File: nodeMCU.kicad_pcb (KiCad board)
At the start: 2 copper layers, 27 x 50 mm, 40 parts, among them J1 USB_B_Micro, J2 Conn_01x15, J3 Conn_01x15, Q1 S8050, Q2 S8050, U1 AP1117-33, U2 CP2102N-A01-GQFN28, U3 ESP-12E

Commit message: PCB Terminado
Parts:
- moved H3 39.7 mm to (158.0, 65.8)
- moved H4 39.7 mm to (134.6, 65.7)
- moved C3 39.5 mm to (141.6, 94.2)
- moved C4 39.5 mm to (143.8, 102.5)
- moved C6 39.5 mm to (141.6, 90.3)
- moved C8 39.5 mm to (136.6, 68.7)
- moved D1 39.5 mm to (138.7, 102.7)
- moved R12 39.5 mm to (155.2, 90.0)
- moved R13 39.5 mm to (136.6, 72.2)
- moved R14 39.5 mm to (136.6, 74.2)
- moved R3 39.5 mm to (149.8, 97.3)
- moved R4 39.5 mm to (144.3, 97.3)
- moved R6 39.5 mm to (140.7, 97.3)
- moved R7 39.5 mm to (153.5, 97.3)
- moved REF** 39.5 mm to (146.2, 73.3)
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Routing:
- net GND: vias 106 -> 107
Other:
- board text added: "Esta placa fue desarrollada en el marco de la materia "Diseño de circuitos impresos" pertenceciente a la Carrera de Especializacion en Sistemas Embebidos de la UBA. Para este proyecto se tomo como premisa usar los mismo tamaños que su original. Es por esto que algunos de los componentes poseen encapsulados de tamaño reducido. Grillas: 1mm, 0.5mm, 0.10mm Vias: 0.30/0.15mm, 0.5/0.3mm Margen: 0.2mm 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"

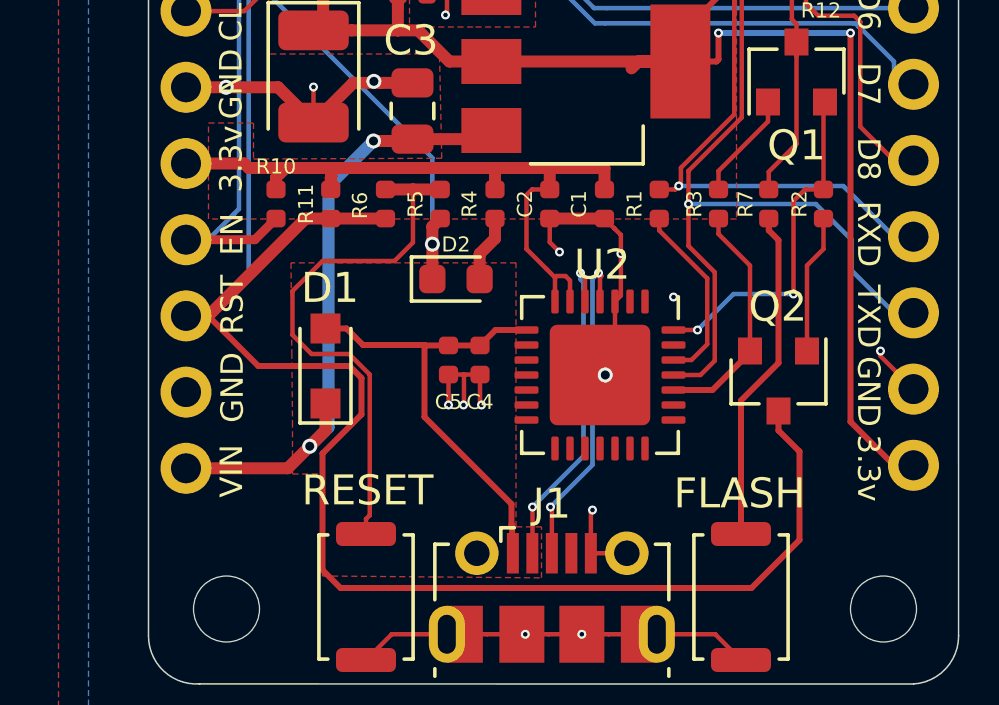
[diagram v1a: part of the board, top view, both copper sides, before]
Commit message: Agrego fiducial
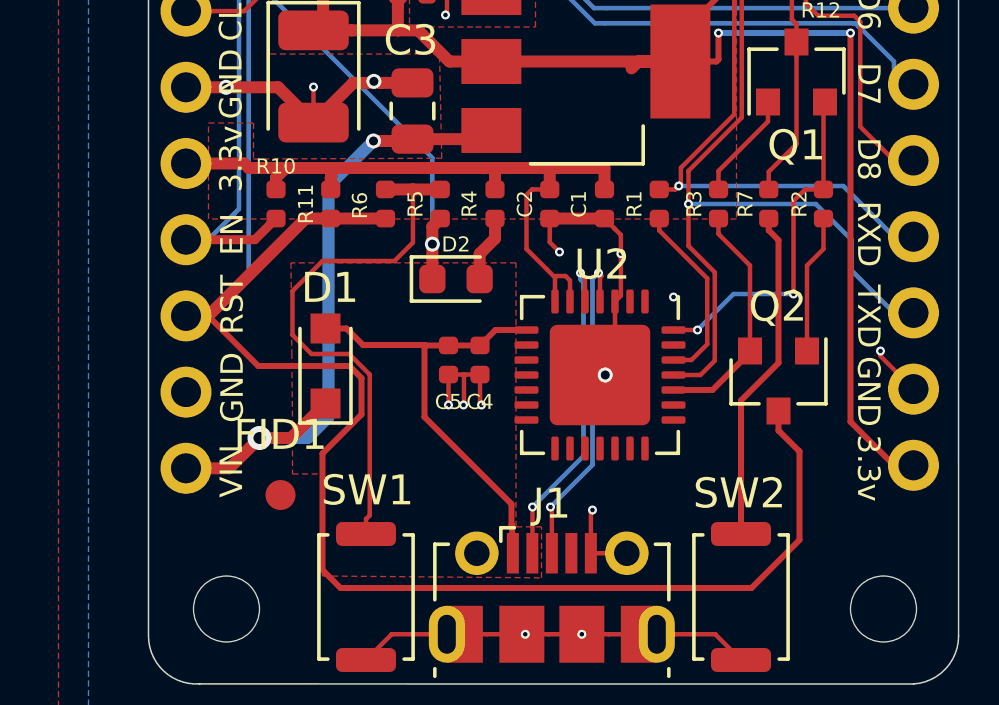
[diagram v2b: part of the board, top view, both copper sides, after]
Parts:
- added FID1: Fiducial, Fiducial:Fiducial_1mm_Mask2mm, F.Cu at (137.2, 107.0)
- renumbered RESET to SW1, FLASH to SW2
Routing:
- net +5V: track 20.5 -> 22.0 mm

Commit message: Terminado el PCB
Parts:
- moved R9 0.16 mm to (156.0, 82.2)
- moved R2 0.13 mm to (155.4, 97.4)
- moved R8 0.07 mm to (156.0, 80.0)
- moved R10 0.05 mm to (137.0, 97.3)

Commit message: Agrego comentarios del Docente
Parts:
- moved H2 7.91 mm to (127.5, 110.5)
- moved H4 7.63 mm to (127.0, 65.0)
- moved J2 7.07 mm to (127.0, 69.5)
- moved C1 7.07 mm to (141.0, 96.3)
- moved C2 7.07 mm to (139.2, 96.3)
- moved C3 7.07 mm to (134.6, 93.2)
- moved C4 7.07 mm to (136.8, 101.5)
- moved C5 7.07 mm to (135.8, 101.5)
- moved C6 7.07 mm to (134.6, 89.3)
- moved C7 7.07 mm to (131.3, 92.0)
- moved C8 7.07 mm to (129.6, 67.7)
- moved D1 7.07 mm to (131.7, 101.7)
- moved D2 7.07 mm to (136.1, 98.8)
- moved FID1 7.07 mm to (130.2, 106.0)
- moved J3 7.07 mm to (151.3, 69.5)
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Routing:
- net /nRST: track 77.2 -> 79.1 mm
- net /GPIO_2: track 4.42 -> 3.12 mm
- net Net-(J1-Pad2): track 11.1 -> 12.2 mm
- net VBUS: track 15.0 -> 15.9 mm
- net /RXD: track 35.0 -> 35.8 mm
- net /GPIO_16: track 50.3 -> 51.0 mm
- net +3V3: track 84.3 -> 85.0 mm
- net Net-(R3-Pad2): track 6.20 -> 6.80 mm
- net /TXD: track 47.9 -> 48.5 mm
- net GND: track 62.8 -> 62.3 mm, vias 107 -> 14
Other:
- board size 27 x 50 mm -> 28 x 51 mm
- rule via_min_size: 0.15 -> 0.5
- board text added: "Esta placa fue desarrollada en el marco de la materia “Diseño de circuitos impresos” pertenceciente a la Carrera de Especializacion en Sistemas Embebidos de la UBA. Para este proyecto se tomo como premisa usar los mismo tamaños que su original. Es por esto que algunos de los componentes poseen encapsulados de tamaño reducido. Grillas: 1mm, 0.5mm, 0.10mm Vias: 0.5/0.3mm Margen: 0.1mm Pistas: 0.4mm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"
- board text added: "HECHO EN ARG"
- board text removed: "Esta placa fue desarrollada en el marco de la materia "Diseño de circuitos impresos" pertenceciente a la Carrera de Especializacion en Sistemas Embebidos de la UBA. Para este proyecto se tomo como premisa usar los mismo tamaños que su original. Es por esto que algunos de los componentes poseen encapsulados de tamaño reducido. Grillas: 1mm, 0.5mm, 0.10mm Vias: 0.30/0.15mm, 0.5/0.3mm Margen: 0.2mm 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"
- board text removed: "HECHO EN ARGENTINA"

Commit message: Correcciones propuestas II
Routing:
- net /SCLK: track 26.5 -> 14.2 mm
- net +3V3: track 85.0 -> 88.1 mm
- net /RXD: track 35.8 -> 38.8 mm
- net /MISO: track 16.0 -> 13.0 mm, vias 0 -> 2
- net /GPIO_5: track 5.09 -> 7.71 mm
- net /GPIO_10: track 20.4 -> 18.0 mm
- net /GPIO_2: track 3.12 -> 5.22 mm
- net /TXD: track 48.5 -> 46.7 mm
- net /nRST: track 79.1 -> 80.4 mm
- net GND: track 62.3 -> 61.3 mm, vias 14 -> 11
- net /CS0: track 13.5 -> 12.8 mm
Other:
- net class Default: clearance 0.1 -> 0.2
- rule trace_clearance: 0.1 -> 0.2

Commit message: Correcciones finales segun el docente
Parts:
- moved REF** 1.70 mm to (139.2, 74.0)
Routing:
- net /SCLK: track 14.2 -> 30.2 mm, vias 0 -> 2
- net /TXD: track 46.7 -> 51.7 mm
- net Net-(J1-Pad3): track 11.3 -> 11.8 mm
- net /nRTS_CP: track 7.97 -> 8.47 mm
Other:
- board text added: "Esta placa fue desarrollada en el marco de la materia “Diseño de circuitos impresos” pertenceciente a la Carrera de Especializacion en Sistemas Embebidos de la UBA. Para este proyecto se tomo como premisa usar los mismo tamaños que su original por ejemplo los encapsulados 0402. Grillas: 1mm, 0.5mm, 0.10mm Vias: 0.5/0.3mm Margen: 0.2 mm Pistas: 0.4mm, 0.2mm, 0.15mm Distancia a borde: 0.1mm Termina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"
- board text removed: "Esta placa fue desarrollada en el marco de la materia “Diseño de circuitos impresos” pertenceciente a la Carrera de Especializacion en Sistemas Embebidos de la UBA. Para este proyecto se tomo como premisa usar los mismo tamaños que su original. Es por esto que algunos de los componentes poseen encapsulados de tamaño reducido. Grillas: 1mm, 0.5mm, 0.10mm Vias: 0.5/0.3mm Margen: 0.1mm Pistas: 0.4mm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"
